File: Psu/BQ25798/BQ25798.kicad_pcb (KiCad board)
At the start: 2 copper layers, 75.2 x 35 mm, 46 parts, among them J1 I2C, J2 IN, J3 UPS, J4 CTRL, J5 BAT, Q1 NMOS, Q2 NMOS, Q3 NMOS, U1 BQ25798

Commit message: Production Values
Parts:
- R8: value 5.24k -> 5.2k; footprint Resistor_SMD:R_0603_1608Metric -> Resistor_SMD:R_0805_2012Metric

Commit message: YARR
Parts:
- removed J1: I2C, Connector_PinHeader_2.54mm:PinHeader_1x02_P2.54mm_Vertical
- removed J4: CTRL, Connector_PinHeader_2.54mm:PinHeader_1x03_P2.54mm_Vertical
- added C25: 10 uF, Capacitor_SMD:C_0603_1608Metric, F.Cu at (137.2, 33.6)
- added C26: 10 uF, Capacitor_SMD:C_0603_1608Metric, F.Cu at (148.1, 29.1)
- added C27: 100nF, Capacitor_SMD:C_0805_2012Metric, F.Cu at (136.1, 49.4)
- added C28: 100nF, Capacitor_SMD:C_0805_2012Metric, F.Cu at (138.8, 47.9)
- added J6: USB_C_Receptacle_USB2.0, Connector_USB:USB_C_Receptacle_HRO_TYPE-C-31-M-12, F.Cu at (127.2, 54.6)
- added R10: 5.1k, Resistor_SMD:R_0603_1608Metric, F.Cu at (129.7, 48.3)
- added R11: 5.1k, Resistor_SMD:R_0603_1608Metric, F.Cu at (133.4, 57.7)
- added R12: 10k Ohm, Resistor_SMD:R_0805_2012Metric, F.Cu at (159.0, 27.0)
- added R13: 22, Resistor_SMD:R_0603_1608Metric, F.Cu at (135.5, 53.5)
- added R14: 22, Resistor_SMD:R_0603_1608Metric, F.Cu at (135.5, 55.4)
- added SW1: KH-6X6X5H-STM, footprints:KH-6X6X5H-STM_SKE, F.Cu at (167.1, 29.2)
- added U2: CH552G, footprints:CH552G, F.Cu at (132.3, 42.4)
- added U3: AMS1117-3.3, Package_TO_SOT_SMD:SOT-223-3_TabPin2, F.Cu at (142.8, 29.2)
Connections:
- net Net-(J2-Pin_1) renamed /VIN
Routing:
- net +3V3: track 0.00 -> 66.8 mm, vias 0 -> 3
- net Net-(U2-RST): track 0.00 -> 46.8 mm, vias 0 -> 2
- net D+: track 0.00 -> 11.7 mm
- net Net-(U1-SCL): track 35.5 -> 46.9 mm
- net D-: track 0.00 -> 9.23 mm
- net Net-(U1-SDA): track 30.8 -> 37.9 mm, vias 1 -> 2
- net Net-(J6-CC1): track 0.00 -> 6.38 mm
- net Net-(J6-D--PadA7): track 0.00 -> 6.14 mm
- net Net-(U1-~{INT}): track 43.8 -> 38.0 mm, vias 3 -> 4
- net Net-(J6-D+-PadA6): track 0.00 -> 5.17 mm
- net Net-(U1-~{CE}): track 41.7 -> 46.2 mm
- net Net-(R12-Pad2): track 0.00 -> 2.67 mm
- net Net-(J6-CC2): track 0.00 -> 2.37 mm
- net Net-(U1-~{QON}): track 38.9 -> 40.9 mm, vias 3 -> 4
- net /VIN: track 51.9 -> 53.4 mm
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
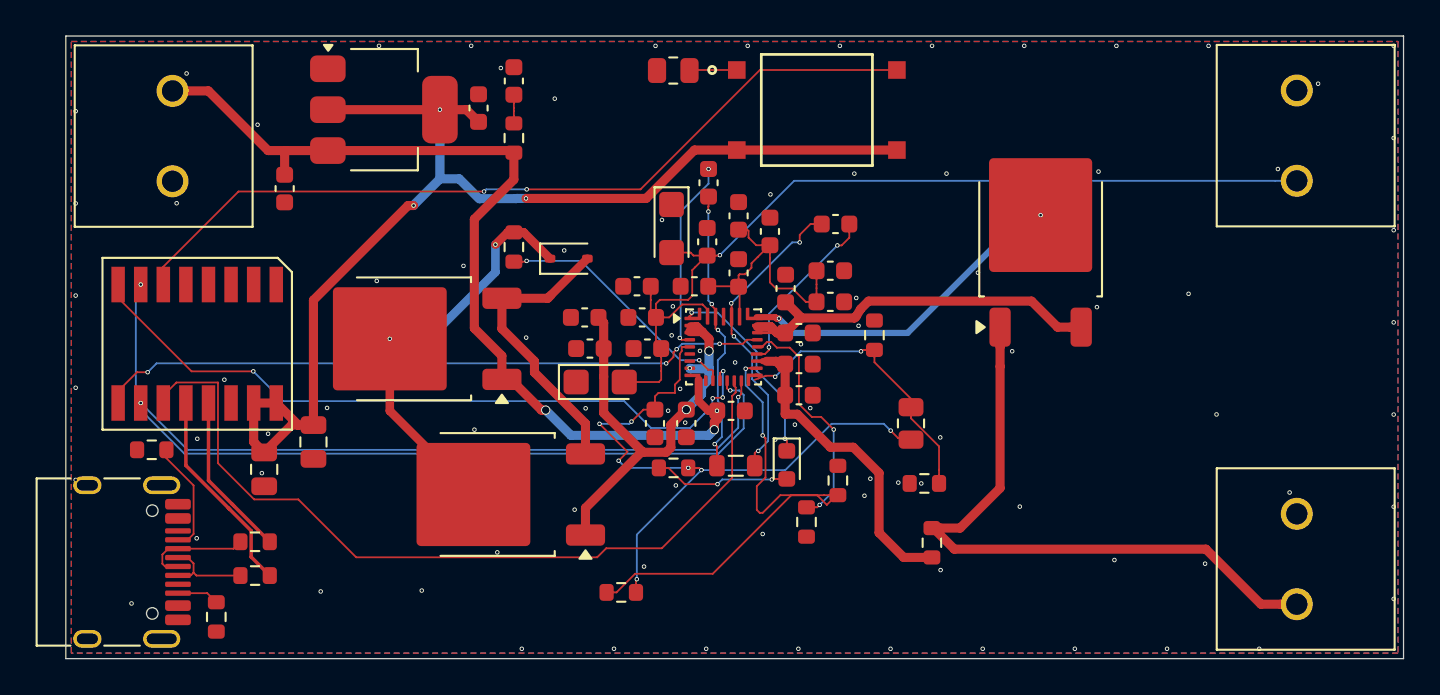
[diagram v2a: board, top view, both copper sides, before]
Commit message: Rework some trace lines for wider with in high amperage environments
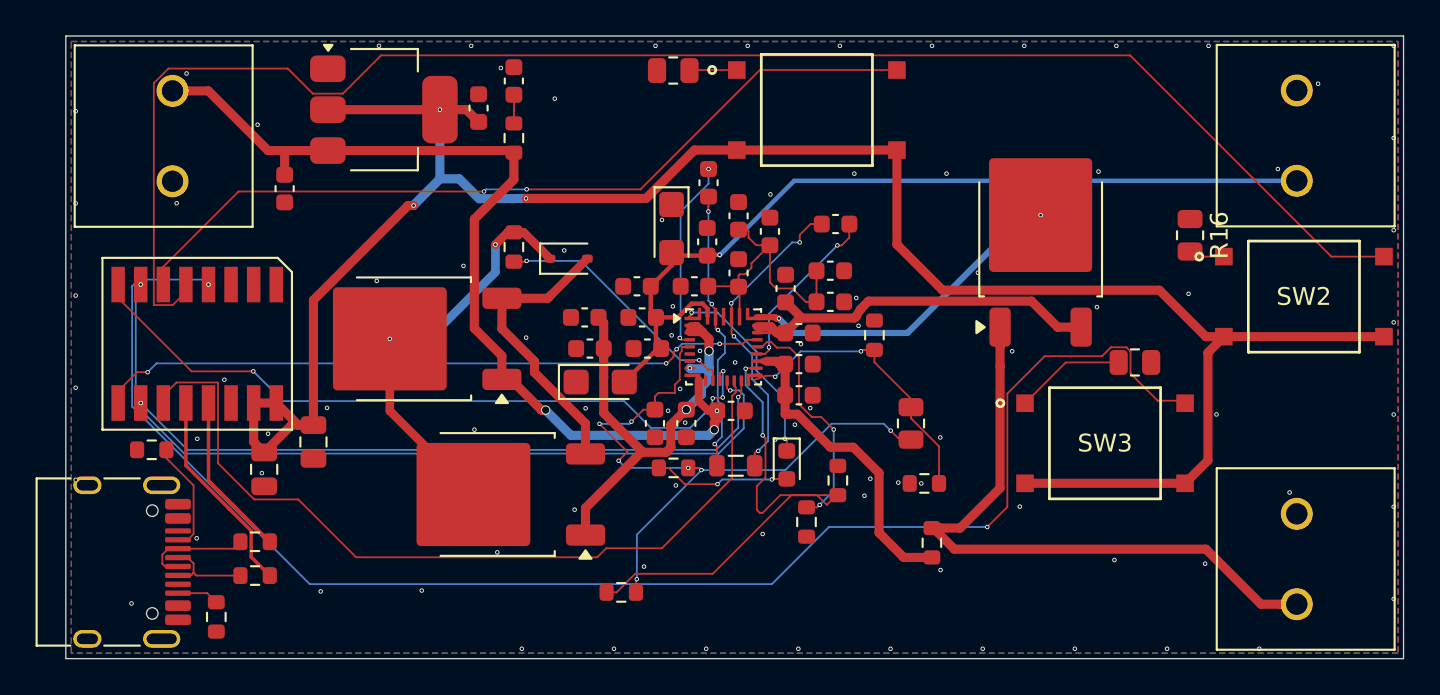
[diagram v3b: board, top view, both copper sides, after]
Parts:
- added R15: 10k Ohm, Resistor_SMD:R_0805_2012Metric, F.Cu at (185.0, 43.4)
- added R16: 10k Ohm, Resistor_SMD:R_0805_2012Metric, F.Cu at (188.1, 36.2)
- added SW2: KH-6X6X5H-STM, footprints:KH-6X6X5H-STM_SKE, F.Cu at (194.5, 39.7)
- added SW3: KH-6X6X5H-STM, footprints:KH-6X6X5H-STM_SKE, F.Cu at (183.3, 47.9)
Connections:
- U2 pad 4: unconnected-(U2-P1.6-Pad4) -> Net-(U2-P1.6)
- U2 pad 5: unconnected-(U2-P1.7-Pad5) -> Net-(U2-P1.7)
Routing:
- net Net-(U2-P1.7): track 0.00 -> 90.6 mm
- net Net-(U2-P1.6): track 0.00 -> 86.2 mm, vias 0 -> 2
- net +3V3: track 66.8 -> 119.7 mm
- net Net-(R15-Pad2): track 0.00 -> 6.22 mm
- net Net-(J3-Pin_1): track 53.9 -> 51.0 mm
- net Net-(R16-Pad2): track 0.00 -> 2.02 mm

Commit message: reroute
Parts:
- moved R3 11.7 mm to (166.2, 50.5), turned to 180 degrees
- moved R5 8.12 mm to (168.4, 44.5), turned to -90 degrees
- moved R7 6.90 mm to (171.2, 47.1), turned to 0 degrees
- moved R9 5.84 mm to (172.2, 44.5), turned to 90 degrees
- moved R8 3.08 mm to (170.4, 44.5)
- moved R6 2.65 mm to (152.6, 37.8)
- moved R4 2.25 mm to (167.0, 48.2)
- moved D2 1.48 mm to (154.4, 38.4), turned to -90 degrees
- moved TH1 1.16 mm to (169.2, 42.0), turned to 0 degrees
- moved D1 0.96 mm to (165.4, 48.2)
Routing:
- net Net-(U1-ILIM_HIZ): track 30.0 -> 11.4 mm
- net Net-(U1-BATP): track 17.8 -> 9.62 mm
- net Net-(U1-PROG): track 13.4 -> 6.67 mm, vias 2 -> 0
- net Net-(U1-TS): track 16.4 -> 10.2 mm
- net /REGN: track 38.0 -> 33.2 mm
- net Net-(D1-K): track 11.5 -> 8.65 mm, vias 2 -> 1
- net Net-(U1-ACDRV1): track 14.3 -> 11.8 mm
- net Net-(D1-A): track 7.69 -> 9.64 mm
- net /VIN: track 53.4 -> 54.4 mm
- net Net-(J5-Pin_1): track 36.1 -> 35.1 mm
- net Net-(U1-~{INT}): track 38.0 -> 38.5 mm
- net Net-(D2-A): track 16.4 -> 15.9 mm
- net Net-(D2-K): track 23.7 -> 24.2 mm
- net GND: vias 90 -> 82
